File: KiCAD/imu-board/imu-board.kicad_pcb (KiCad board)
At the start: 2 copper layers, 8 parts, among them J1 AVR-TPI-6, J2 A-2004-3-4-LP-N-R, U1 ATtiny10-MA, U2 ISM330DHCX

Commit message: fiddling with placement in develop
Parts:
- removed U1: ATtiny10-MA, Package_DFN_QFN:DFN-8-1EP_2x2mm_P0.5mm_EP0.9x1.5mm
- added U3: ATmega168A-MM, Package_DFN_QFN:QFN-28-1EP_4x4mm_P0.45mm_EP2.4x2.4mm, F.Cu at (53.9, 59.1)
- J1: footprint Connector_PinHeader_1.00mm:PinHeader_2x03_P1.00mm_Vertical -> Connector_PinHeader_1.00mm:PinHeader_2x03_P1.00mm_Vertical_SMD; moved to B.Cu
- moved J2 39.0 mm to (41.4, 56.9), turned to -90 degrees
- moved R1 12.5 mm to (58.7, 56.9), turned to 0 degrees
- moved C1 11.3 mm to (60.3, 61.3), turned to 0 degrees
- moved R2 10.5 mm to (60.5, 56.9)
- moved J1 10.5 mm to (54.2, 59.1), turned to 180 degrees
- moved U2 9.24 mm to (59.4, 58.9)
- moved C2 8.76 mm to (57.7, 61.2), turned to 0 degrees
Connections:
- J2 pad 3: Net-(U1-PB2) -> /PB1
- R2 pad 2: /PB1 -> Net-(U2-SCL)
- U2 pad P13: /PB1 -> Net-(U2-SCL)
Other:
- board outline added: 23 x 8 mm

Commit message: test 12x8 mm placement
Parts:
- added J3: AVR-ISP-6, Connector_PinHeader_1.00mm:PinHeader_1x06_P1.00mm_Vertical, F.Cu at (52.5, 56.2)
- J1: value AVR-TPI-6 -> Conn_01x04; footprint Connector_PinHeader_1.00mm:PinHeader_2x03_P1.00mm_Vertical_SMD -> Connector_PinHeader_1.27mm:PinHeader_1x04_P1.27mm_Vertical; moved to F.Cu
- moved J1 3.18 mm to (51.2, 58.1), turned to 0 degrees
- moved R1 2.44 mm to (60.8, 55.7), turned to 180 degrees
- moved U3 1.71 mm to (55.4, 60.0)
- moved C2 1.31 mm to (59.0, 61.1)
- moved C1 0.42 mm to (60.7, 61.1)
- moved R2 0.41 mm to (60.9, 56.7)
- moved U2 0.40 mm to (59.8, 58.9)
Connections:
- J1 pad 1: /PB0 -> unconnected-(J1-Pin_1-Pad1)
- J1 pad 2: VCC -> unconnected-(J1-Pin_2-Pad2)
- J1 pad 3: /PB1 -> unconnected-(J1-Pin_3-Pad3)
- J2 pad 2: /PB3 -> unconnected-(J2-Pad2)
- J2 pad 3: /PB1 -> unconnected-(J2-Pad3)
- R1 pad 2: /PB0 -> Net-(U2-SDA/SDI/SDO)
- U2 pad P14: /PB0 -> Net-(U2-SDA/SDI/SDO)
- U3 pad 18: Net-(U3-GND-Pad18) -> GND
- U3 pad 29: Net-(U3-GND-Pad18) -> GND
- U3 pad 4: Net-(U3-GND-Pad18) -> GND
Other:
- board size 23 x 8 mm -> 12 x 8 mm

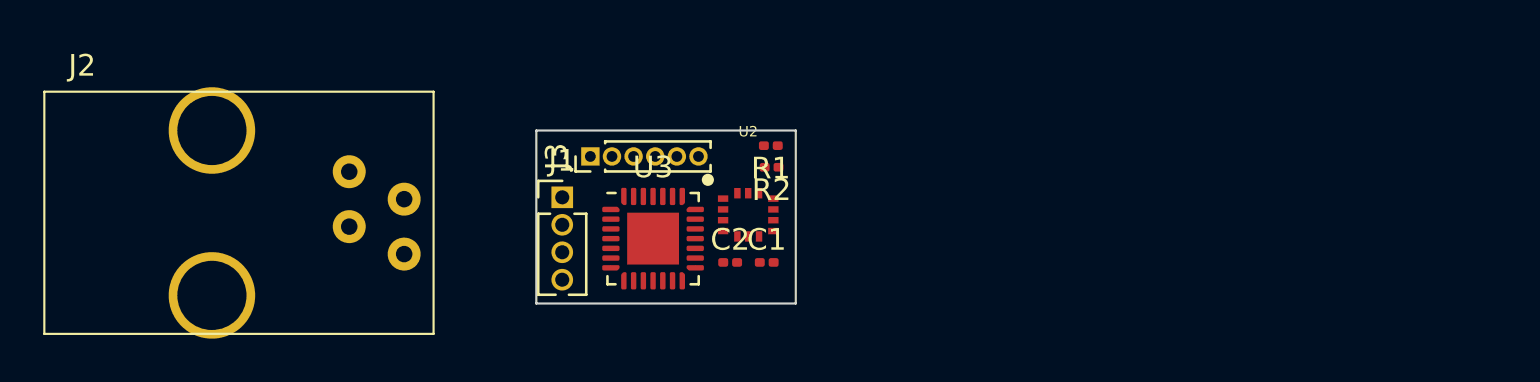
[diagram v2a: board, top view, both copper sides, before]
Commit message: candidate layout without RJ connector included
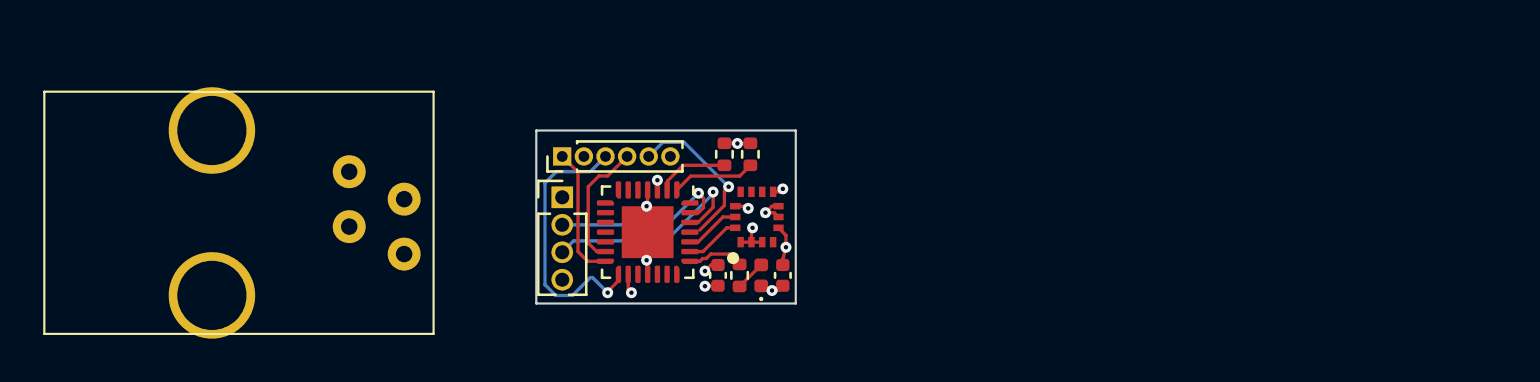
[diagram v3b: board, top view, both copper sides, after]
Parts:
- removed R2: 4.7k, Resistor_SMD:R_0201_0603Metric
- added D1: LED, LED_SMD:LED_0402_1005Metric, F.Cu at (60.4, 61.7)
- added JP1: JPR2, Resistor_SMD:R_0402_1005Metric, F.Cu at (58.7, 56.1)
- added JP2: JPR2, Resistor_SMD:R_0402_1005Metric, F.Cu at (59.9, 56.1)
- C1, C2: footprint Capacitor_SMD:C_0201_0603Metric -> Capacitor_SMD:C_0402_1005Metric
- R1: value 4.7k -> R_US; footprint Resistor_SMD:R_0201_0603Metric -> Resistor_SMD:R_0402_1005Metric
- moved R1 6.17 mm to (59.4, 61.7), turned to -90 degrees
- moved J3 1.30 mm to (51.2, 56.2)
- moved C1 0.96 mm to (61.4, 61.7), turned to -90 degrees
- moved C2 0.82 mm to (58.4, 61.7), turned to -90 degrees
- moved U2 0.41 mm to (60.2, 59.0), turned to 90 degrees
- moved U3 0.39 mm to (55.1, 59.7), turned to -90 degrees
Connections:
- J1 pad 1: unconnected-(J1-Pin_1-Pad1) -> VCC
- J1 pad 2: unconnected-(J1-Pin_2-Pad2) -> /TXD
- J1 pad 3: unconnected-(J1-Pin_3-Pad3) -> /RXD
- J1 pad 4: unconnected-(J1-Pin_4-Pad4) -> GND
- J2 pad 2: unconnected-(J2-Pad2) -> /TXD
- J2 pad 3: unconnected-(J2-Pad3) -> /RXD
- J3 pad 1: unconnected-(J3-MISO-Pad1) -> /MISO
- J3 pad 3: unconnected-(J3-SCK-Pad3) -> /SCK
- J3 pad 4: unconnected-(J3-MOSI-Pad4) -> /MOSI
- J3 pad 5: unconnected-(J3-~{RST}-Pad5) -> /nRESET
- R1 pad 1: VCC -> Net-(U3-PC3)
- R1 pad 2: Net-(U2-SDA/SDI/SDO) -> Net-(D1-A)
- U2 pad P13: Net-(U2-SCL) -> /SCL
- U2 pad P14: Net-(U2-SDA/SDI/SDO) -> /SDA
- U3 pad 1: unconnected-(U3-PD3-Pad1) -> Net-(JP2-A)
- U3 pad 13: unconnected-(U3-PB3-Pad13) -> /MOSI
- U3 pad 14: unconnected-(U3-PB4-Pad14) -> /MISO
- U3 pad 15: unconnected-(U3-PB5-Pad15) -> /SCK
- U3 pad 2: unconnected-(U3-PD4-Pad2) -> Net-(JP1-A)
- U3 pad 22: unconnected-(U3-PC3-Pad22) -> Net-(U3-PC3)
- U3 pad 23: unconnected-(U3-PC4-Pad23) -> /SDA
- U3 pad 24: unconnected-(U3-PC5-Pad24) -> /SCL
- U3 pad 25: unconnected-(U3-~{RESET}/PC6-Pad25) -> /nRESET
- U3 pad 26: unconnected-(U3-PD0-Pad26) -> /RXD
- U3 pad 27: unconnected-(U3-PD1-Pad27) -> /TXD
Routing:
- net /SCK: track 0.00 -> 12.5 mm, vias 0 -> 1
- net /RXD: track 0.00 -> 10.3 mm, vias 0 -> 1
- net GND: track 0.00 -> 10.1 mm, vias 0 -> 7
- net /TXD: track 0.00 -> 8.40 mm, vias 0 -> 1
- net /nRESET: track 0.00 -> 7.37 mm, vias 0 -> 1
- net /MISO: track 0.00 -> 6.16 mm
- net /MOSI: track 0.00 -> 5.95 mm
- net VCC: track 0.00 -> 5.41 mm, vias 0 -> 6
- net Net-(JP2-A): track 0.00 -> 3.87 mm
- net Net-(JP1-A): track 0.00 -> 3.36 mm
- net Net-(U3-PC3): track 0.00 -> 2.64 mm
- net /SCL: track 0.00 -> 2.58 mm
- net /SDA: track 0.00 -> 2.56 mm
- net Net-(D1-A): track 0.00 -> 1.41 mm
- added copper zone on In1.Cu, net GND
- added copper zone on In2.Cu, net VCC
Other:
- copper layers 2 -> 4

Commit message: close to final IMU layout
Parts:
- removed J2: A-2004-3-4-LP-N-R, my_RJ:A-2004-3-4-LP
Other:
- board size 12 x 8 mm -> 16 x 8 mm
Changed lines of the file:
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@@
 (kicad_pcb (version 20221018) (generator pcbnew)
   (general
-    (thickness 1.6)
+    (thickness 0.8)
   )
   (paper "A4")
@@
       (layer "dielectric 1" (type "prepreg") (thickness 0.1) (material "FR4") (epsilon_r 4.5) (loss_tangent 0.02))
       (layer "In1.Cu" (type "copper") (thickness 0.035))
-      (layer "dielectric 2" (type "core") (thickness 1.24) (material "FR4") (epsilon_r 4.5) (loss_tangent 0.02))
+      (layer "dielectric 2" (type "core") (thickness 0.44) (material "FR4") (epsilon_r 4.5) (loss_tangent 0.02))
       (layer "In2.Cu" (type "copper") (thickness 0.035))
       (layer "dielectric 3" (type "prepreg") (thickness 0.1) (material "FR4") (epsilon_r 4.5) (loss_tangent 0.02))
@@
     (pad_to_mask_clearance 0)
     (pcbplotparams
-      (layerselection 0x00010fc_ffffffff)
+      (layerselection 0x00010f8_ffffffff)
       (plot_on_all_layers_selection 0x0000000_00000000)
       (disableapertmacros false)
@@
       (outputformat 1)
       (mirror false)
-      (drillshape 1)
+      (drillshape 0)
       (scaleselection 1)
-      (outputdirectory "")
+      (outputdirectory "gerber/")
     )
   )
@@
     )
   )
-  (footprint "my_RJ:A-2004-3-4-LP" (layer "F.Cu")
-    (at 41.35 56.905 -90)
-    (property "CatNo" "AE10381-ND")
-    (property "Sheetfile" "imu-board.kicad_sch")
-    (property "Sheetname" "")
-    (property "ki_description" "RJ connector, 4P4C (4 positions 4 connected), RJ9/RJ10/RJ22")
-    (property "ki_keywords" "4P4C RJ socket connector")
-    (attr through_hole)
-    (fp_text reference "J2" (at -4.905 12.35) (layer "F.SilkS") hide
-        (effects (font (size 1.016 1.016) (thickness 0.1524)))
-    )
-    (fp_text value "A-2004-3-4-LP-N-R" (at 0 1 -90 unlocked) (layer "F.Fab") hide
-        (effects (font (size 1 1) (thickness 0.15)))
-    )
-    (fp_text user "${REFERENCE}" (at 0 2.5 -90 unlocked) (layer "F.Fab")
-        (effects (font (size 1 1) (thickness 0.15)))
-    )
-    (fp_line (start -3.7 -3.9) (end 7.5 -3.9)
-      (stroke (width 0.1) (type default)) (layer "F.SilkS"))
-    (fp_line (start -3.7 14.1) (end -3.7 -3.9)
-      (stroke (width 0.1) (type default)) (layer "F.SilkS"))
-    (fp_line (start 7.5 -3.9) (end 7.5 14.1)
-      (stroke (width 0.1) (type default)) (layer "F.SilkS"))
-    (fp_line (start 7.5 14.1) (end -3.7 14.1)
-      (stroke (width 0.1) (type default)) (layer "F.SilkS"))
-    (pad "1" thru_hole circle (at 0 0 270) (size 1.524 1.524) (drill 0.762) (layers "*.Cu" "*.Mask")
-      (net 1 "VCC") (pintype "passive"))
-    (pad "2" thru_hole circle (at 1.27 -2.54 270) (size 1.524 1.524) (drill 0.762) (layers "*.Cu" "*.Mask")
-      (net 5 "/TXD") (pintype "passive"))
-    (pad "3" thru_hole circle (at 2.54 0 270) (size 1.524 1.524) (drill 0.762) (layers "*.Cu" "*.Mask")
-      (net 6 "/RXD") (pintype "passive"))
-    (pad "4" thru_hole circle (at 3.81 -2.54 270) (size 1.524 1.524) (drill 0.762) (layers "*.Cu" "*.Mask")
-      (net 2 "GND") (pintype "passive"))
-    (pad "5" thru_hole circle (at -1.905 6.35 270) (size 4 4) (drill 3.2) (layers "*.Cu" "*.Mask"))
-    (pad "6" thru_hole circle (at 5.72 6.35 270) (size 4 4) (drill 3.2) (layers "*.Cu" "*.Mask"))
-  )
   (footprint "Capacitor_SMD:C_0402_1005Metric" (layer "F.Cu")
     (at 61.4 61.7 -90)
@@
     )
   )
-  (gr_line (start 62 63) (end 50 63)
-    (stroke (width 0.1) (type default)) (layer "Edge.Cuts"))
-  (gr_line (start 62 55) (end 62 63)
-    (stroke (width 0.1) (type default)) (layer "Edge.Cuts"))
-  (gr_line (start 50 55) (end 62 55)
-    (stroke (width 0.1) (type default)) (layer "Edge.Cuts"))
-  (gr_line (start 50 55) (end 50 63)
-    (stroke (width 0.1) (type default)) (layer "Edge.Cuts"))
+  (gr_line (start 61.6 63) (end 50.2 63)
+    (stroke (width 0.1) (type default)) (layer "Edge.Cuts"))
+  (gr_line (start 46.4 62.5) (end 47 62.5)
+    (stroke (width 0.1) (type default)) (layer "Edge.Cuts"))
+  (gr_arc (start 62 62.6) (mid 61.882843 62.882843) (end 61.6 63)
+    (stroke (width 0.1) (type default)) (layer "Edge.Cuts"))
+  (gr_line (start 49.6 57.5) (end 49 57.5)
+    (stroke (width 0.1) (type default)) (layer "Edge.Cuts"))
+  (gr_line (start 47 62.5) (end 47 62)
+    (stroke (width 0.1) (type default)) (layer "Edge.Cuts"))
+  (gr_arc (start 46 57.9) (mid 46.117157 57.617157) (end 46.4 57.5)
+    (stroke (width 0.1) (type default)) (layer "Edge.Cuts"))
+  (gr_line (start 62 55.4) (end 62 62.6)
+    (stroke (width 0.1) (type default)) (layer "Edge.Cuts"))
+  (gr_line (start 50 62.8) (end 50 62.7)
+    (stroke (width 0.1) (type default)) (layer "Edge.Cuts"))
+  (gr_line (start 46 57.9) (end 46 62.1)
+    (stroke (width 0.1) (type default)) (layer "Edge.Cuts"))
+  (gr_arc (start 61.6 55) (mid 61.882843 55.117157) (end 62 55.4)
+    (stroke (width 0.1) (type default)) (layer "Edge.Cuts"))
+  (gr_line (start 47 58) (end 47 57.5)
+    (stroke (width 0.1) (type default)) (layer "Edge.Cuts"))
+  (gr_line (start 49 58) (end 47 58)
+    (stroke (width 0.1) (type default)) (layer "Edge.Cuts"))
+  (gr_arc (start 50.2 63) (mid 50.058579 62.941421) (end 50 62.8)
+    (stroke (width 0.1) (type default)) (layer "Edge.Cuts"))
+  (gr_line (start 47 57.5) (end 46.4 57.5)
+    (stroke (width 0.1) (type default)) (layer "Edge.Cuts"))
+  (gr_line (start 47 62) (end 49 62)
+    (stroke (width 0.1) (type default)) (layer "Edge.Cuts"))
+  (gr_line (start 49 62) (end 49 62.5)
+    (stroke (width 0.1) (type default)) (layer "Edge.Cuts"))
+  (gr_arc (start 49.8 62.5) (mid 49.941421 62.558579) (end 50 62.7)
+    (stroke (width 0.1) (type default)) (layer "Edge.Cuts"))
+  (gr_line (start 50.4 55) (end 61.6 55)
+    (stroke (width 0.1) (type default)) (layer "Edge.Cuts"))
+  (gr_arc (start 50 57.1) (mid 49.882843 57.382843) (end 49.6 57.5)
+    (stroke (width 0.1) (type default)) (layer "Edge.Cuts"))
+  (gr_arc (start 50 55.4) (mid 50.117157 55.117157) (end 50.4 55)
+    (stroke (width 0.1) (type default)) (layer "Edge.Cuts"))
+  (gr_arc (start 46.4 62.5) (mid 46.117157 62.382843) (end 46 62.1)
+    (stroke (width 0.1) (type default)) (layer "Edge.Cuts"))
+  (gr_line (start 49 57.5) (end 49 58)
+    (stroke (width 0.1) (type default)) (layer "Edge.Cuts"))
+  (gr_line (start 50 55.4) (end 50 57.1)
+    (stroke (width 0.1) (type default)) (layer "Edge.Cuts"))
+  (gr_line (start 49 62.5) (end 49.8 62.5)
+    (stroke (width 0.1) (type default)) (layer "Edge.Cuts"))
+  (gr_line (start 47 58) (end 49 58)
+    (stroke (width 0.15) (type default)) (layer "User.2"))
+  (gr_line (start 49 62) (end 49 62.5)
+    (stroke (width 0.15) (type default)) (layer "User.2"))
+  (gr_line (start 47 62) (end 49 62)
+    (stroke (width 0.15) (type default)) (layer "User.2"))
+  (gr_line (start 47 62.5) (end 47 62)
+    (stroke (width 0.15) (type default)) (layer "User.2"))
+  (gr_line (start 49 58) (end 49 57.5)
+    (stroke (width 0.15) (type default)) (layer "User.2"))
+  (gr_line (start 47 58) (end 47 57.5)
+    (stroke (width 0.15) (type default)) (layer "User.2"))
   (dimension (type orthogonal) (layer "User.2")
     (pts (xy 50 55) (xy 62 55))
@@
       (effects (font (size 1 1) (thickness 0.15)))
     )
+    (format (prefix "") (suffix "") (units 3) (units_format 1) (precision 1))
+    (style (thickness 0.15) (arrow_length 1.27) (text_position_mode 0) (extension_height 0.58642) (extension_offset 0.5) keep_text_aligned)
+  )
+  (dimension (type orthogonal) (layer "User.2")
+    (pts (xy 46 62.5) (xy 62 63))
+    (height 3)
+    (orientation 0)
+    (gr_text "16.0 mm" (at 54 64.35) (layer "User.2")
+      (effects (font (size 1 1) (thickness 0.15)))
+    )
+    (format (prefix "") (suffix "") (units 3) (units_format 1) (precision 1))
+    (style (thickness 0.15) (arrow_length 1.27) (text_position_mode 0) (extension_height 0.58642) (extension_offset 0.5) keep_text_aligned)
+  )
+  (dimension (type orthogonal) (layer "User.2")
+    (pts (xy 46 57.5) (xy 46 62.5))
+    (height -3)
+    (orientation 1)
+    (gr_text "5.0 mm" (at 41.85 60 90) (layer "User.2")
+      (effects (font (size 1 1) (thickness 0.15)))
+    )

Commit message: IMU and adapter ready to go?
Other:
- board text added: "FNIRS IMU V1.0 1/2024 ESH"
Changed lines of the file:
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@@
   (gr_line (start 47 58) (end 47 57.5)
     (stroke (width 0.15) (type default)) (layer "User.2"))
+  (gr_text "FNIRS IMU V1.0\n1/2024 ESH" (at 59.4 61.6) (layer "B.SilkS")
+    (effects (font (size 1 1) (thickness 0.15)) (justify left bottom mirror))
+  )
   (dimension (type orthogonal) (layer "User.2")
     (pts (xy 50 55) (xy 62 55))
